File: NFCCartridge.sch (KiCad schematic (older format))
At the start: 8 parts, among them J1 Cartridge Connector, U1 W25Q128, U2 ST25DVxxx

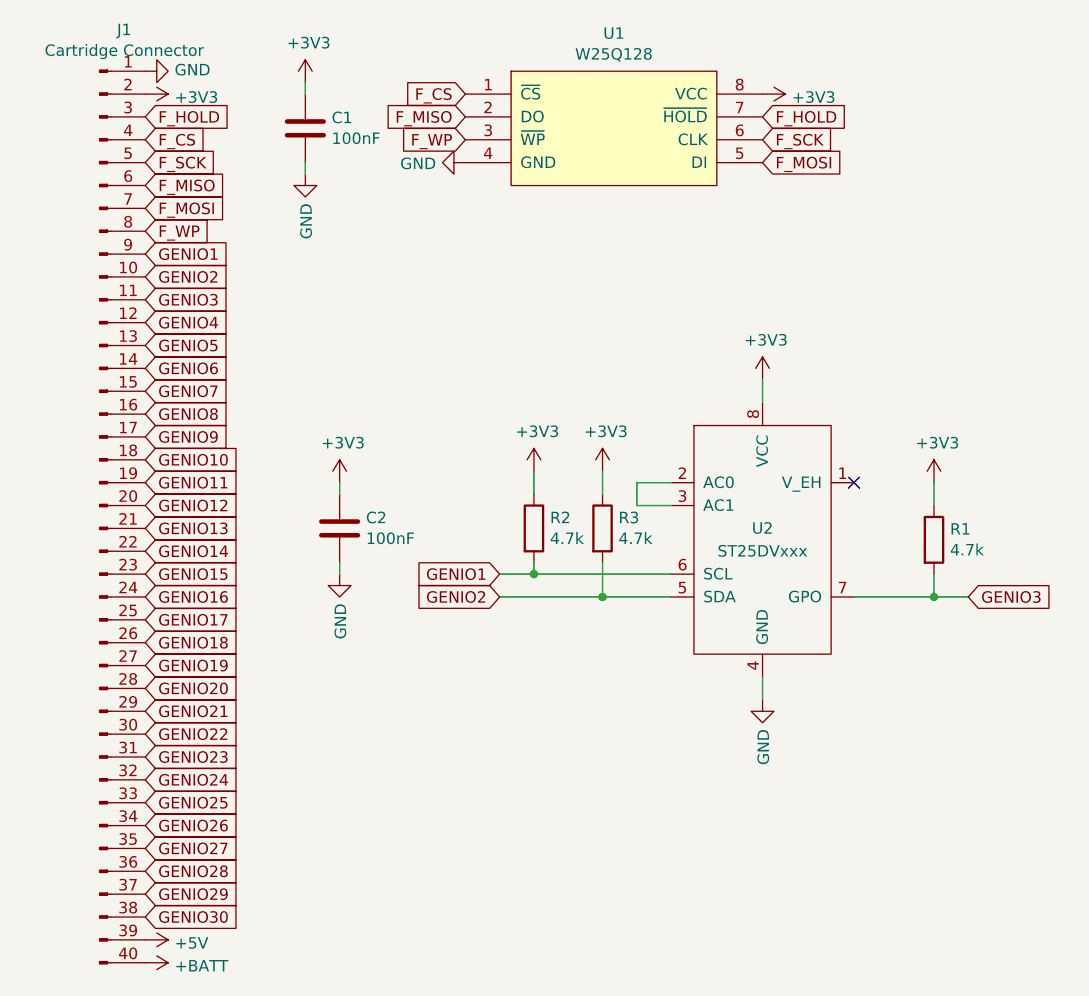
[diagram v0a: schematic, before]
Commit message: Fixed error in cartridge connector pin assignments
Updated to version 1.2
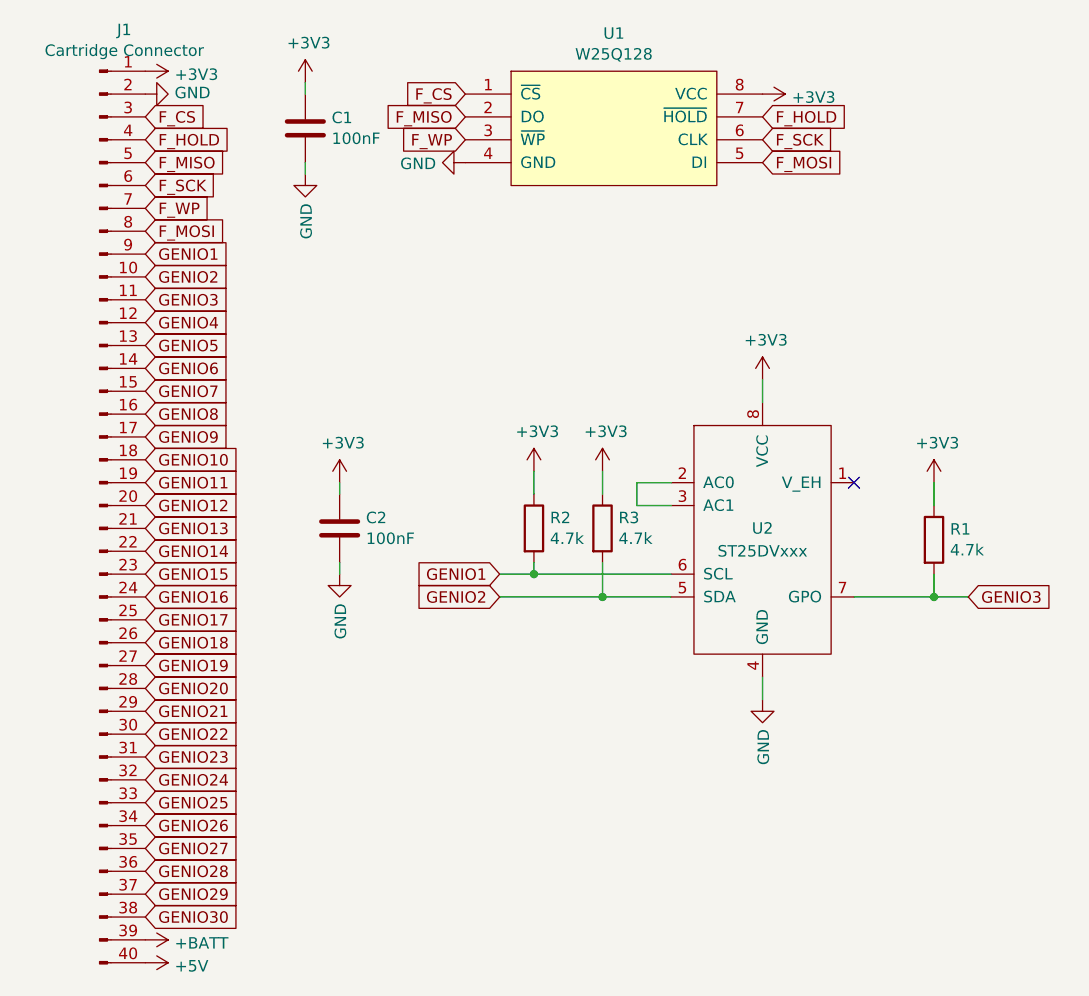
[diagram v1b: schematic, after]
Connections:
- net +3V3: now also J1.1 (Pin_1); no longer J1.2 (Pin_2)
- net +5V: now also J1.40 (Pin_40); no longer J1.39 (Pin_39)
- net +BATT: now also J1.39 (Pin_39); no longer J1.40 (Pin_40)
- net F_CS: now also J1.3 (Pin_3); no longer J1.4 (Pin_4)
- net F_HOLD: now also J1.4 (Pin_4); no longer J1.3 (Pin_3)
- net F_MISO: now also J1.5 (Pin_5); no longer J1.6 (Pin_6)
- net F_MOSI: now also J1.8 (Pin_8); no longer J1.7 (Pin_7)
- net F_SCK: now also J1.6 (Pin_6); no longer J1.5 (Pin_5)
- net F_WP: now also J1.7 (Pin_7); no longer J1.8 (Pin_8)
- net GND: now also J1.2 (Pin_2); no longer J1.1 (Pin_1)
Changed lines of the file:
@@
 L power:GND #PWR01
 U 1 1 5D9C2B6C
-P 1300 1100
-F 0 "#PWR01" H 1300 850 50  0001 C CNN
-F 1 "GND" V 1305 972 50  0000 R CNN
-F 2 "" H 1300 1100 50  0001 C CNN
-F 3 "" H 1300 1100 50  0001 C CNN
-	1    1300 1100
+P 1300 1200
+F 0 "#PWR01" H 1300 950 50  0001 C CNN
+F 1 "GND" V 1305 1072 50  0000 R CNN
+F 2 "" H 1300 1200 50  0001 C CNN
+F 3 "" H 1300 1200 50  0001 C CNN
+	1    1300 1200
 	0    -1   -1   0
 $EndComp
@@
 L power:+3V3 #PWR02
 U 1 1 5D9C3D7F
-P 1300 1200
-F 0 "#PWR02" H 1300 1050 50  0001 C CNN
-F 1 "+3V3" V 1315 1328 50  0000 L CNN
-F 2 "" H 1300 1200 50  0001 C CNN
-F 3 "" H 1300 1200 50  0001 C CNN
-	1    1300 1200
+P 1300 1100
+F 0 "#PWR02" H 1300 950 50  0001 C CNN
+F 1 "+3V3" V 1315 1228 50  0000 L CNN
+F 2 "" H 1300 1100 50  0001 C CNN
+F 3 "" H 1300 1100 50  0001 C CNN
+	1    1300 1100
 	0    1    1    0
 $EndComp
+Text GLabel 1300 1400 2    50   Input ~ 0
+F_HOLD
 Text GLabel 1300 1300 2    50   Input ~ 0
-F_HOLD
-Text GLabel 1300 1400 2    50   Input ~ 0
 F_CS
+Text GLabel 1300 1600 2    50   Input ~ 0
+F_SCK
 Text GLabel 1300 1500 2    50   Input ~ 0
-F_SCK
-Text GLabel 1300 1600 2    50   Input ~ 0
 F_MISO
+Text GLabel 1300 1800 2    50   Input ~ 0
+F_MOSI
 Text GLabel 1300 1700 2    50   Input ~ 0
-F_MOSI
-Text GLabel 1300 1800 2    50   Input ~ 0
 F_WP
 $Comp
 L power:+BATT #PWR06
 U 1 1 5D9C7330
+P 1300 4900
+F 0 "#PWR06" H 1300 4750 50  0001 C CNN
+F 1 "+BATT" V 1315 5028 50  0000 L CNN
+F 2 "" H 1300 4900 50  0001 C CNN
+F 3 "" H 1300 4900 50  0001 C CNN
+	1    1300 4900
+	0    1    1    0
+$EndComp
+$Comp
+L power:+5V #PWR05
+U 1 1 5D9C7C1B
 P 1300 5000
-F 0 "#PWR06" H 1300 4850 50  0001 C CNN
-F 1 "+BATT" V 1315 5128 50  0000 L CNN
+F 0 "#PWR05" H 1300 4850 50  0001 C CNN
+F 1 "+5V" V 1315 5128 50  0000 L CNN
 F 2 "" H 1300 5000 50  0001 C CNN
 F 3 "" H 1300 5000 50  0001 C CNN
@@
 	0    1    1    0
 $EndComp
-$Comp
-L power:+5V #PWR05
-U 1 1 5D9C7C1B
-P 1300 4900
-F 0 "#PWR05" H 1300 4750 50  0001 C CNN
-F 1 "+5V" V 1315 5028 50  0000 L CNN
-F 2 "" H 1300 4900 50  0001 C CNN
-F 3 "" H 1300 4900 50  0001 C CNN
-	1    1300 4900
-	0    1    1    0
-$EndComp
